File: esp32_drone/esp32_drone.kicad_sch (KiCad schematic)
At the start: 33 parts, among them J1 Conn_01x07_Socket, J2 Conn_01x07_Socket, J3 B2B-PH-K-S_LF__SN_, M1 Motor_DC, M2 Motor_DC, M3 Motor_DC, M4 Motor_DC, Q2 IRLML2502TRPBF, Q3 IRLML2502TRPBF, Q4 IRLML2502TRPBF, Q5 IRLML2502TRPBF, U1 MPU-6050, U2 AP2204K-ADJ

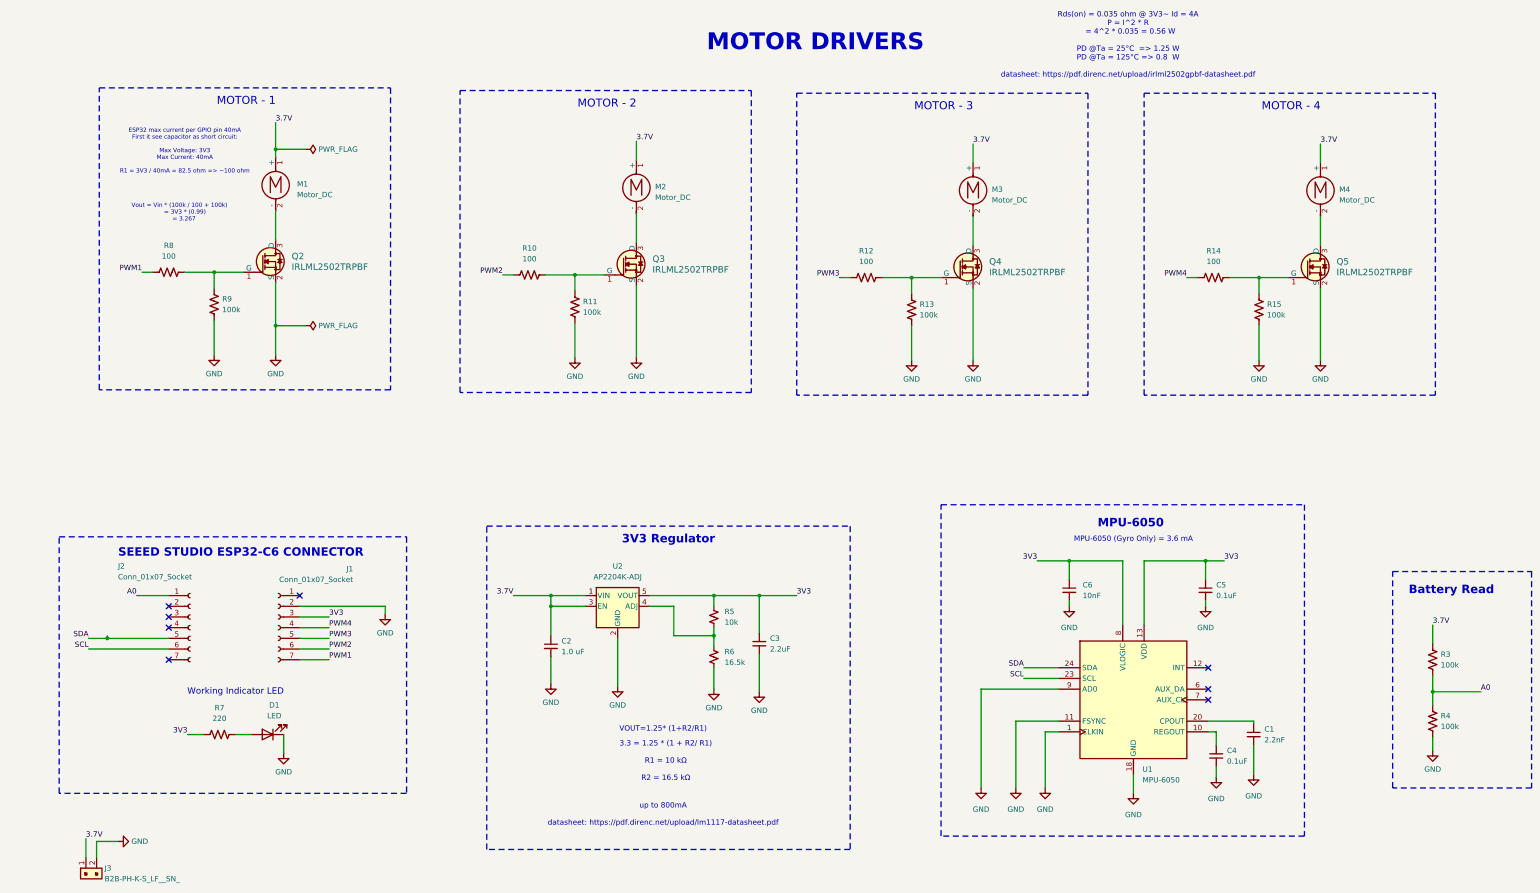
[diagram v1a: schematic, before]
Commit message: finished without flyback diode
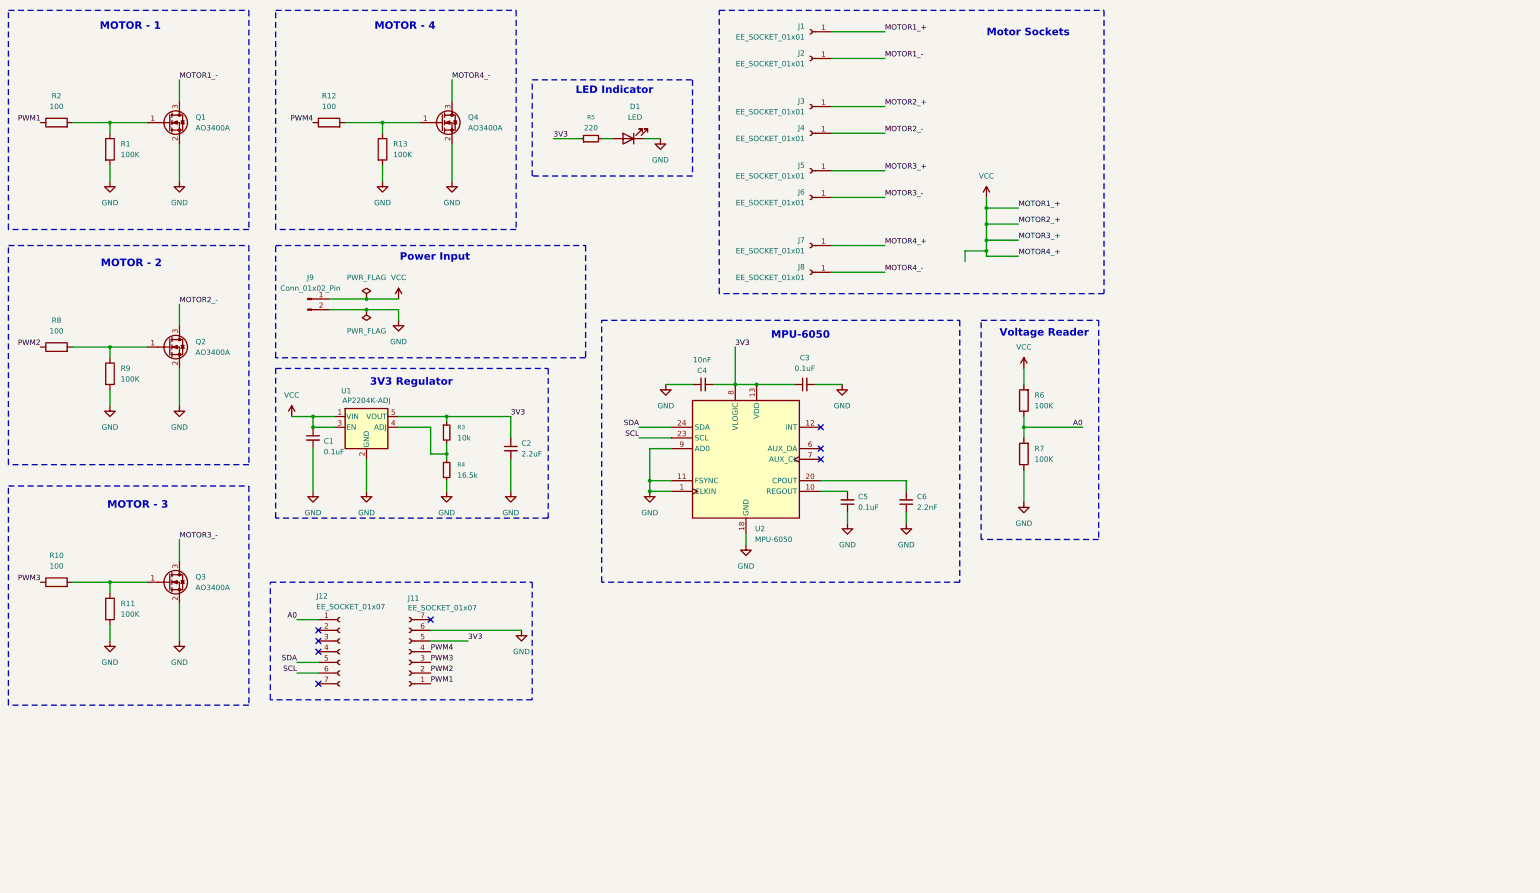
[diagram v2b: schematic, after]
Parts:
- removed J1, J2: Conn_01x07_Socket, Connector_PinSocket_2.54mm:PinSocket_1x07_P2.54mm_Vertical, symbol Connector:Conn_01x07_Socket
- removed J3: B2B-PH-K-S_LF__SN_, Connector_JST:JST_PH_S2B-PH-K_1x02_P2.00mm_Horizontal, symbol dk_Rectangular-Connectors-Headers-Male-Pins:B2B-PH-K-S_LF__SN_
- removed M1, M2, M3, M4: Motor_DC, Connector_Wire:SolderWire-0.1sqmm_1x02_P3.6mm_D0.4mm_OD1mm, symbol Motor:Motor_DC
- removed Q2, Q3, Q4, Q5: IRLML2502TRPBF, digikey-footprints:SOT-23-3, symbol dk_Transistors-FETs-MOSFETs-Single:IRLML2502TRPBF
- removed R10, R12, R14, R8: 100, Resistor_SMD:R_0603_1608Metric, symbol Device:R_US
- removed R11, R13, R15, R3, R4, R9: 100k, Resistor_SMD:R_0603_1608Metric, symbol Device:R_US
- removed R5: 10k, Resistor_SMD:R_1206_3216Metric, symbol Device:R_Small_US
- removed R6: 16.5k, Resistor_SMD:R_1206_3216Metric, symbol Device:R_Small_US
- removed R7: 220, Resistor_SMD:R_0805_2012Metric, symbol Device:R_US
- removed U1: MPU-6050, Sensor_Motion:InvenSense_QFN-24_4x4mm_P0.5mm, symbol Sensor_Motion:MPU-6050
- removed U2: AP2204K-ADJ, Package_TO_SOT_SMD:SOT-23-5, symbol Regulator_Linear:AP2204K-ADJ
- added J1, J2, J3, J4, J5, J6, J7, J8: EE_SOCKET_01x01, TestPoint:TestPoint_Pad_D1.5mm, symbol EE_TERMINAL:EE_SOCKET_01x01
- added J11, J12: EE_SOCKET_01x07, Connector_PinSocket_2.54mm:PinSocket_1x07_P2.54mm_Vertical, symbol EE_TERMINAL:EE_SOCKET_01x07
- added J9: Conn_01x02_Pin, Connector_JST:JST_EH_S2B-EH_1x02_P2.50mm_Horizontal, symbol Connector:Conn_01x02_Pin
- added Q1, Q2, Q3, Q4: AO3400A, Package_TO_SOT_SMD:SOT-23, symbol Transistor_FET:AO3400A
- added R1, R11, R13, R6, R7, R9: 100K, Resistor_SMD:R_0603_1608Metric_Pad0.98x0.95mm_HandSolder, symbol EE_RESISTOR:EE_RES_1/4W_THT
- added R10, R12, R2, R8: 100, Resistor_SMD:R_0603_1608Metric_Pad0.98x0.95mm_HandSolder, symbol EE_RESISTOR:EE_RES_1/4W_THT
- added R3: 10k, Resistor_SMD:R_0805_2012Metric_Pad1.20x1.40mm_HandSolder, symbol Device:R_Small
- added R4: 16.5k, Resistor_SMD:R_1206_3216Metric_Pad1.30x1.75mm_HandSolder, symbol Device:R_Small
- added R5: 220, Resistor_SMD:R_0805_2012Metric_Pad1.20x1.40mm_HandSolder, symbol Device:R_Small
- added U1: AP2204K-ADJ, Package_TO_SOT_SMD:SOT-23-5, symbol Regulator_Linear:AP2204K-ADJ
- added U2: MPU-6050, Sensor_Motion:InvenSense_QFN-24_4x4mm_P0.5mm, symbol Sensor_Motion:MPU-6050
- C1: value 2.2nF -> 0.1uF; footprint Capacitor_SMD:C_0402_1005Metric -> Capacitor_SMD:C_0805_2012Metric_Pad1.18x1.45mm_HandSolder
- C2: value 1.0 uF -> 2.2uF; footprint Capacitor_SMD:C_0603_1608Metric -> Capacitor_SMD:C_0603_1608Metric_Pad1.08x0.95mm_HandSolder
- C3: value 2.2uF -> 0.1uF; footprint Capacitor_SMD:C_0402_1005Metric -> Capacitor_SMD:C_0805_2012Metric_Pad1.18x1.45mm_HandSolder
- C4: value 0.1uF -> 10nF; footprint Capacitor_SMD:C_0603_1608Metric -> Capacitor_SMD:C_1206_3216Metric_Pad1.33x1.80mm_HandSolder
- C5: footprint Capacitor_SMD:C_0603_1608Metric -> Capacitor_SMD:C_0805_2012Metric_Pad1.18x1.45mm_HandSolder
- C6: value 10nF -> 2.2nF; footprint Capacitor_SMD:C_0402_1005Metric -> Capacitor_SMD:C_0805_2012Metric_Pad1.18x1.45mm_HandSolder
- D1: footprint LED_SMD:LED_Everlight-SMD3528_3.5x2.8mm_67-21ST -> LED_SMD:LED_0805_2012Metric_Pad1.15x1.40mm_HandSolder
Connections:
- net 3.7V is gone; now on net 3V3: C2.1
- net 3V3: now also C4.1, J11.5 (Pin_5), R3.1, R5.1, U1.5 (VOUT), U2.13 (VDD), U2.8 (VLOGIC); no longer C5.1, C6.1
- net A0: now also J12.1 (Pin_1), R6.1, R7.2
- net GND: now also C5.1, C6.1, J11.6 (Pin_6), J9.2 (Pin_2), Q1.2 (S), Q2.2 (S), Q3.2 (S), Q4.2 (S), R1.2, R11.2, R13.2, R4.2, R7.1, R9.2, U1.2 (GND), U2.1 (CLKIN), U2.11 (FSYNC), U2.18 (GND), U2.9 (AD0); no longer C5.2, C6.2
- net PWM1: now also J11.1 (Pin_1), R2.1
- net PWM2: now also J11.2 (Pin_2), R8.1
- net PWM3: now also J11.3 (Pin_3), R10.1
- net PWM4: now also J11.4 (Pin_4), R12.1
- net SCL: now also J12.6 (Pin_6), U2.23 (SCL)
- net SDA: now also J12.5 (Pin_5), U2.24 (SDA)
- net VCC: now reaches C1.1
- net VCC: now also J1.1 (Pin_1), J3.1 (Pin_1), J5.1 (Pin_1), J7.1 (Pin_1), J9.1 (Pin_1), R6.2, U1.1 (VIN), U1.3 (EN)
- net at D1.2 (A): now also R5.2
- new net: Q2.1 (G), R8.2, R9.1
- new net: R3.2, R4.1, U1.4 (ADJ)
- new net: C6.2, U2.20 (CPOUT)
- new net: Q4.1 (G), R12.2, R13.1
- new net: Q3.1 (G), R10.2, R11.1
- new net: C5.2, U2.10 (REGOUT)
- new net: Q1.1 (G), R1.1, R2.2
- new net MOTOR1_-: J2.1 (Pin_1), Q1.3 (D)
- new net MOTOR2_-: J4.1 (Pin_1), Q2.3 (D)
- new net MOTOR3_-: J6.1 (Pin_1), Q3.3 (D)
- new net MOTOR4_-: J8.1 (Pin_1), Q4.3 (D)
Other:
- note added: "LED Indicator"
- note added: "Motor Sockets"
- note added: "Power Input"
- note added: "Voltage Reader"
- note removed: "3.3 = 1.25 * (1 + R2/ R1) R1 = 10 kΩ R2 = 16.5 kΩ"
- note removed: "Battery Read"
- note removed: "ESP32 max current per GPIO pin 40mA First it see capacitor as short circuit: Max Voltage: 3V3 Max Current: 40mA R1 = 3V3 / 40mA = 82.5 ohm => ~100 ohm"
- note removed: "MOTOR DRIVERS"
- note removed: "MPU-6050 (Gyro Only) = 3.6 mA"
- note removed: "Rds(on) = 0.035 ohm @ 3V3~ Id = 4A P = I^2 * R = 4^2 * 0.035 = 0.56 W PD @Ta = 25°C => 1.25 W PD @Ta = 125°C => 0.8 W datasheet: https://pdf.direnc.net/upload/irlml2502gpbf-datasheet.pdf"
- note removed: "SEEED STUDIO ESP32-C6 CONNECTOR"
- note removed: "VOUT=1.25* (1+R2/R1)"
- note removed: "Vout = Vin * (100k / 100 + 100k) = 3V3 * (0.99) = 3.267"
- note removed: "Working Indicator LED"
- note removed: "up to 800mA datasheet: https://pdf.direnc.net/upload/lm1117-datasheet.pdf"
- company: Atik Electronic -> (none)
- title: ESP32 Drone  -> (none)

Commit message: finished routing
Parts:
- added D2, D3, D4, D5: UF4007, Diode_SMD:D_SOD-323_HandSoldering, symbol EE_DIODE:EE_UF4007
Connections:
- net GND: now also D2.2 (A), D3.2 (A), D4.2 (A), D5.2 (A)
- net MOTOR1_-: now also D2.1 (K)
- net MOTOR2_-: now also D4.1 (K)
- net MOTOR3_-: now also D5.1 (K)
- net MOTOR4_-: now also D3.1 (K)

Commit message: finished last product
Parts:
- J1, J2, J3, J4, J5, J6, J7, J8: footprint TestPoint:TestPoint_Pad_D1.5mm -> TestPoint:TestPoint_THTPad_D2.0mm_Drill1.0mm
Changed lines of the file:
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@@
 			)
 		)
-		(property "Footprint" "TestPoint:TestPoint_Pad_D1.5mm"
+		(property "Footprint" "TestPoint:TestPoint_THTPad_D2.0mm_Drill1.0mm"
 			(at 209.55 21.59 0)
 			(effects
@@
 			)
 		)
-		(property "Footprint" "TestPoint:TestPoint_Pad_D1.5mm"
+		(property "Footprint" "TestPoint:TestPoint_THTPad_D2.0mm_Drill1.0mm"
 			(at 209.55 27.94 0)
 			(effects
@@
 			)
 		)
-		(property "Footprint" "TestPoint:TestPoint_Pad_D1.5mm"
+		(property "Footprint" "TestPoint:TestPoint_THTPad_D2.0mm_Drill1.0mm"
 			(at 209.55 54.61 0)
 			(effects
@@
 			)
 		)
-		(property "Footprint" "TestPoint:TestPoint_Pad_D1.5mm"
+		(property "Footprint" "TestPoint:TestPoint_THTPad_D2.0mm_Drill1.0mm"
 			(at 209.55 78.74 0)
 			(effects
@@
 			)
 		)
-		(property "Footprint" "TestPoint:TestPoint_Pad_D1.5mm"
+		(property "Footprint" "TestPoint:TestPoint_THTPad_D2.0mm_Drill1.0mm"
 			(at 209.55 60.96 0)
 			(effects
@@
 			)
 		)
-		(property "Footprint" "TestPoint:TestPoint_Pad_D1.5mm"
+		(property "Footprint" "TestPoint:TestPoint_THTPad_D2.0mm_Drill1.0mm"
 			(at 209.55 39.37 0)
 			(effects
@@
 			)
 		)
-		(property "Footprint" "TestPoint:TestPoint_Pad_D1.5mm"
+		(property "Footprint" "TestPoint:TestPoint_THTPad_D2.0mm_Drill1.0mm"
 			(at 209.55 72.39 0)
 			(effects
@@
 			)
 		)
-		(property "Footprint" "TestPoint:TestPoint_Pad_D1.5mm"
+		(property "Footprint" "TestPoint:TestPoint_THTPad_D2.0mm_Drill1.0mm"
 			(at 209.55 45.72 0)
 			(effects

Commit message: updated mpu6050 footprint
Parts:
- U2: footprint Sensor_Motion:InvenSense_QFN-24_4x4mm_P0.5mm -> Package_DFN_QFN:QFN-24-1EP_4x4mm_P0.5mm_EP2.7x2.6mm
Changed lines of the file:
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@@
 			)
 		)
-		(property "Footprint" "Sensor_Motion:InvenSense_QFN-24_4x4mm_P0.5mm"
+		(property "Footprint" "Package_DFN_QFN:QFN-24-1EP_4x4mm_P0.5mm_EP2.7x2.6mm"
 			(at 194.31 143.51 0)
 			(effects
